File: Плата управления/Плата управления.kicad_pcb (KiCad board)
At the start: 2 copper layers, 66 x 58.4 mm, 65 parts, among them J1 Conn_01x10, J2 Conn_01x10, J3 Conn_01x02, J4 A, J5 B, J6 C, U1 LMV7239M5, U2 LMV324, U3 ISO1050DUB, U5 STM32F071V8Tx, U6 AS5047D, U7 AD8210

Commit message: Питание с (lib_symbols
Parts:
- added C21: 10u, Capacitor_SMD:C_1210_3225Metric_Pad1.33x2.70mm_HandSolder, F.Cu at (131.6, 93.0)
- added C22: 470n, Capacitor_SMD:C_0805_2012Metric_Pad1.18x1.45mm_HandSolder, F.Cu at (134.6, 92.5)
- added C23: 100n, Capacitor_SMD:C_0603_1608Metric_Pad1.08x0.95mm_HandSolder, F.Cu at (135.9, 88.4)
- added C24: 100n, Capacitor_SMD:C_0603_1608Metric_Pad1.08x0.95mm_HandSolder, F.Cu at (145.8, 88.2)
- added C25: 4.7u, Capacitor_SMD:C_0805_2012Metric_Pad1.18x1.45mm_HandSolder, F.Cu at (145.8, 96.3)
- added C26: 100n, Capacitor_SMD:C_0603_1608Metric_Pad1.08x0.95mm_HandSolder, F.Cu at (149.1, 91.9)
- added C27: 22u, Capacitor_SMD:C_1210_3225Metric_Pad1.33x2.70mm_HandSolder, F.Cu at (151.6, 92.7)
- added D7: TPS55165QPWPRQ1, Package_SO:HTSSOP-20-1EP_4.4x6.5mm_P0.65mm_EP3.4x6.5mm, F.Cu at (140.8, 91.7)
- added L1: 4.7u, Inductor_SMD:L_Murata_LQH55DN_5.7x5.0mm, F.Cu at (140.7, 83.6)
- added R28: 100k, Resistor_SMD:R_0603_1608Metric_Pad0.98x0.95mm_HandSolder, F.Cu at (147.3, 91.9)
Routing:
- net Net-(D7-L1): track 0.00 -> 9.26 mm
- net Net-(D7-L2): track 0.00 -> 8.99 mm
- net Net-(D7-VOS_FB): track 0.00 -> 7.43 mm
- net Net-(D7-PG): track 0.00 -> 3.90 mm
- net Net-(D7-BST1): track 0.00 -> 2.31 mm
- net Net-(D7-BST2): track 0.00 -> 2.16 mm
- net GND: track 0.00 -> 1.70 mm, vias 0 -> 1
- added copper zone on F.Cu, net GND
- added copper zone on F.Cu, net Net-(D7-IGN)
- added copper zone on F.Cu, net Net-(D7-VOUT)
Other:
- board size 66 x 58.4 mm -> 112.1 x 58.4 mm

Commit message: Питанипе с TPS55165QPWPRQ1
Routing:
- net Net-(D7-IGN): track 0.00 -> 4.06 mm
- net GND: track 1.70 -> 5.58 mm
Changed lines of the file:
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@@
   (gr_arc (start 116.205 94.615) (mid 113.015789 108.665562) (end 104.14 120.015)
     (stroke (width 0.1) (type default)) (layer "Edge.Cuts"))
+  (segment (start 131.572 94.565) (end 127.939 94.565) (width 0.5) (layer "F.Cu") (net 1))
   (segment (start 143.7675 93.3) (end 144.862 93.3) (width 0.25) (layer "F.Cu") (net 1))
   (segment (start 144.862 93.3) (end 145.288 93.726) (width 0.25) (layer "F.Cu") (net 1))
+  (segment (start 127.939 94.565) (end 127.762 94.742) (width 0.5) (layer "F.Cu") (net 1))
   (via (at 145.288 93.726) (size 0.8) (drill 0.4) (layers "F.Cu" "B.Cu") (net 1))
+  (segment (start 131.572 91.44) (end 127.508 91.44) (width 0.5) (layer "F.Cu") (net 168))
   (segment (start 136.398 83.566) (end 135.89 84.074) (width 0.5) (layer "F.Cu") (net 169))
   (segment (start 137.8675 89.41) (end 136.8925 89.41) (width 0.25) (layer "F.Cu") (net 169))

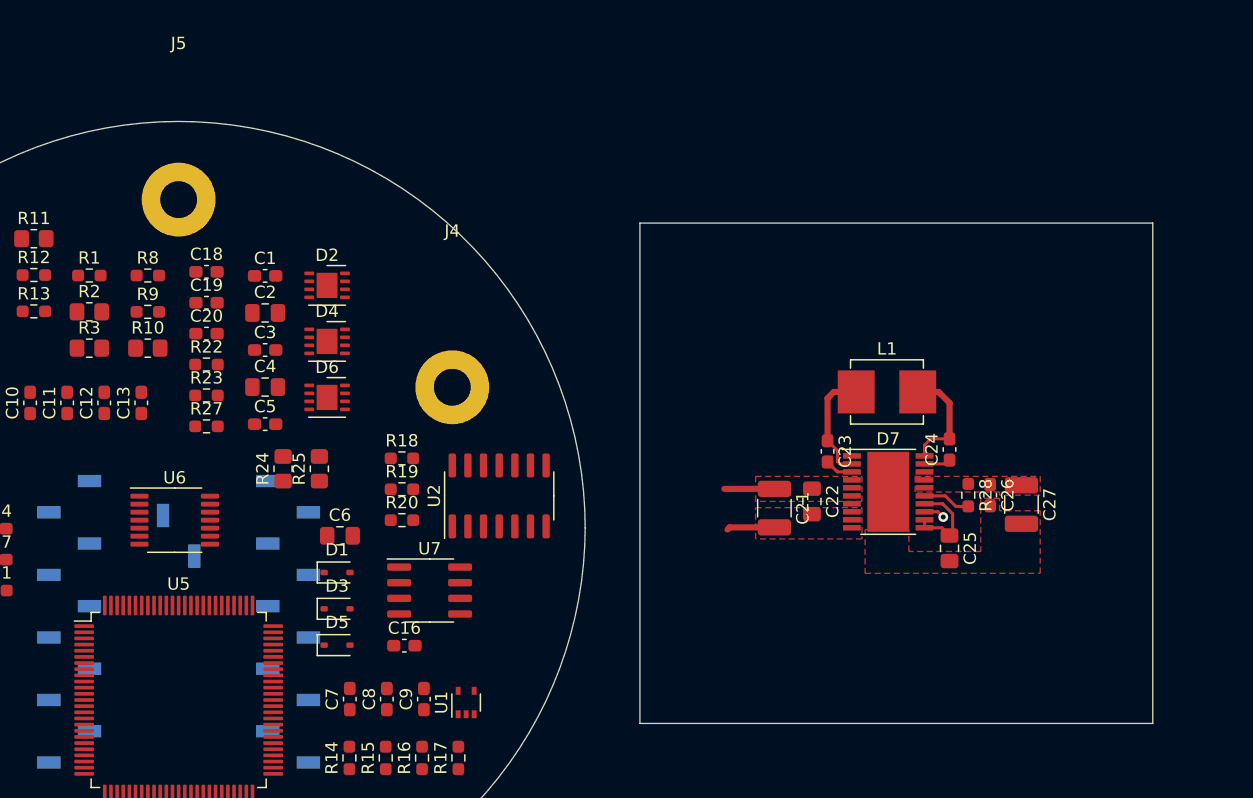
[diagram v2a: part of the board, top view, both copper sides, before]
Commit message: Поенял усилитель измерительный AD8210 на automotive исполнение INA283AID
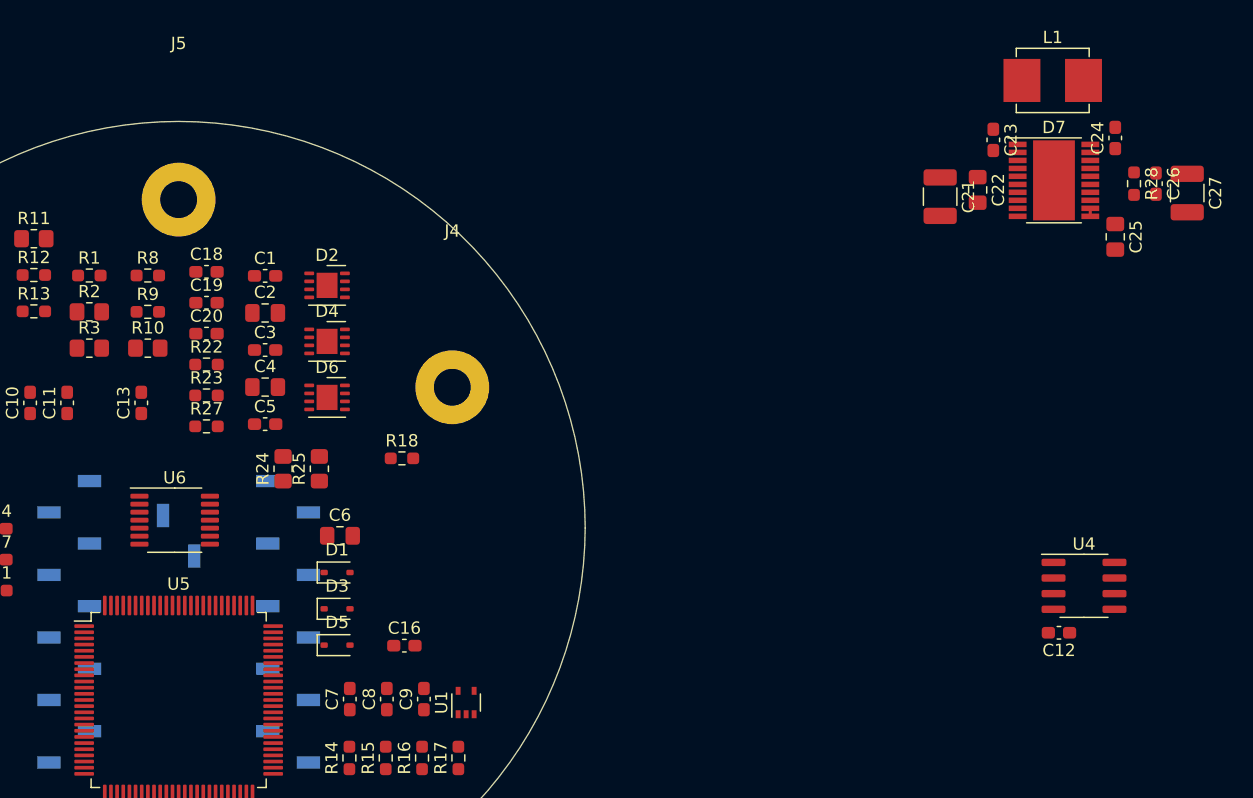
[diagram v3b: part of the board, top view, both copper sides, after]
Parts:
- removed R19: 1.6k, Resistor_SMD:R_0603_1608Metric_Pad0.98x0.95mm_HandSolder
- removed R20: 120, Resistor_SMD:R_0603_1608Metric_Pad0.98x0.95mm_HandSolder
- removed U2: LMV324, Package_SO:SOIC-14_3.9x8.7mm_P1.27mm
- removed U7: AD8210, Package_SO:SOIC-8_3.9x4.9mm_P1.27mm
- added U4: INA283, Package_SO:SOIC-8_3.9x4.9mm_P1.27mm, F.Cu at (156.7, 99.3)
- C12: value 56p -> 0.1u
- C16: value 0.1u -> 56p
- R18: value 1k -> 120
- moved C12 79.8 mm to (154.7, 103.1), turned to 180 degrees
- moved C25 28.7 mm to (159.3, 71.0)
- moved D7 28.7 mm to (154.3, 66.4)
- moved C24 28.7 mm to (159.3, 62.9)
- moved C23 28.7 mm to (149.4, 63.1)
- moved R28 28.7 mm to (160.8, 66.6)
- moved C22 28.7 mm to (148.1, 67.2)
- moved L1 28.7 mm to (154.2, 58.3)
- moved C21 28.7 mm to (145.0, 67.7)
- moved C26 28.7 mm to (162.6, 66.6)
- moved C27 28.7 mm to (165.1, 67.4)
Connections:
- C12 pad 1: DC_Current_MCU -> +3.3V
- C16 pad 1: GND -> DC_Current_MCU
- C16 pad 2: +5V -> GND
- D7 pad 21: GND -> (no net)
- R15 pad 1: +5V -> +3.3V
- R16 pad 2: Net-(R16-Pad2) -> DC_Current_MCU
- R18 pad 2: Net-(R16-Pad2) -> DC_Current_MCU
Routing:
- net Net-(D7-L1): track 9.26 -> 0.00 mm
- net Net-(D7-L2): track 8.99 -> 0.00 mm
- net Net-(D7-VOS_FB): track 7.43 -> 1.01 mm
- net GND: track 5.58 -> 0.00 mm, vias 1 -> 0
- net Net-(D7-IGN): track 4.06 -> 0.00 mm
- net Net-(D7-PG): track 3.90 -> 0.00 mm
- net Net-(D7-BST1): track 2.31 -> 0.00 mm
- net Net-(D7-BST2): track 2.16 -> 0.44 mm
- removed copper zone on F.Cu, net GND
- removed copper zone on F.Cu, net Net-(D7-IGN)
- removed copper zone on F.Cu, net Net-(D7-VOUT)
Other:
- board size 112.1 x 58.4 mm -> 66 x 58.4 mm

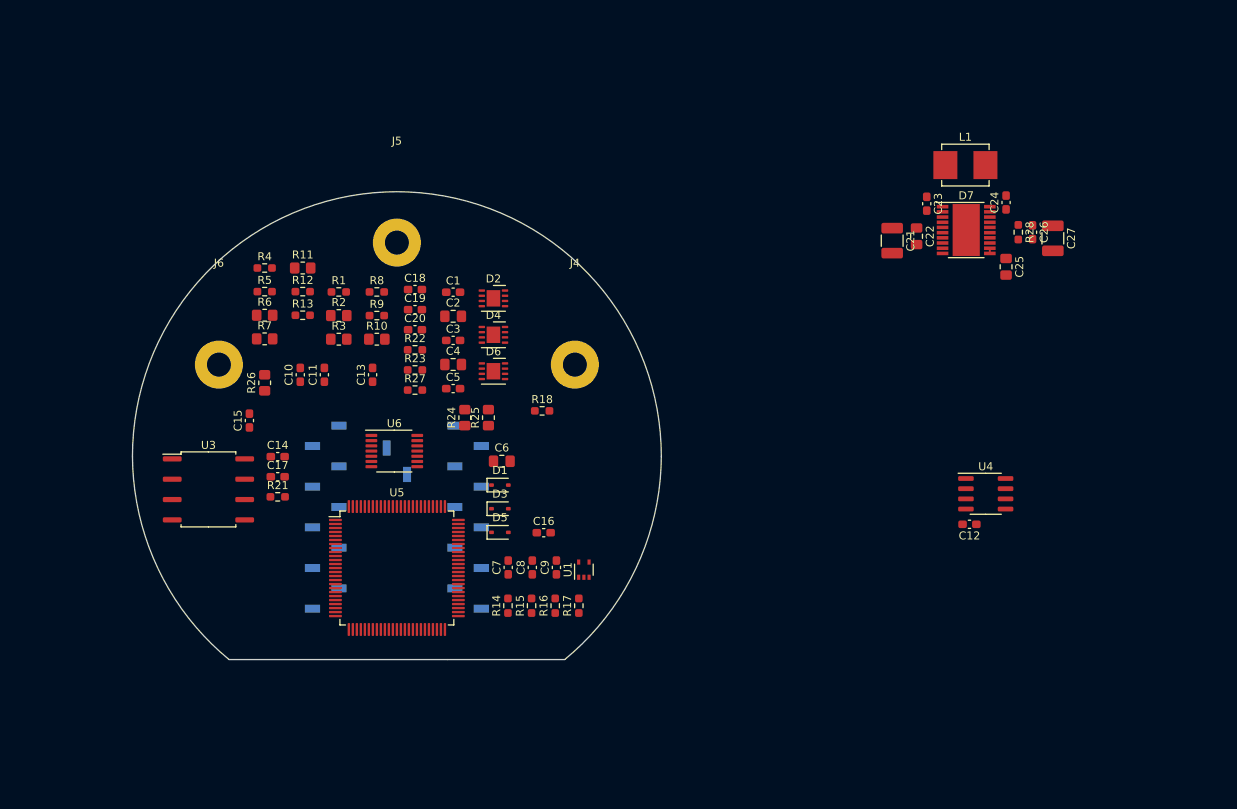
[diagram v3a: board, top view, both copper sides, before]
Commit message: Добавил питание 12В в automotive испорлнении и 3.3В
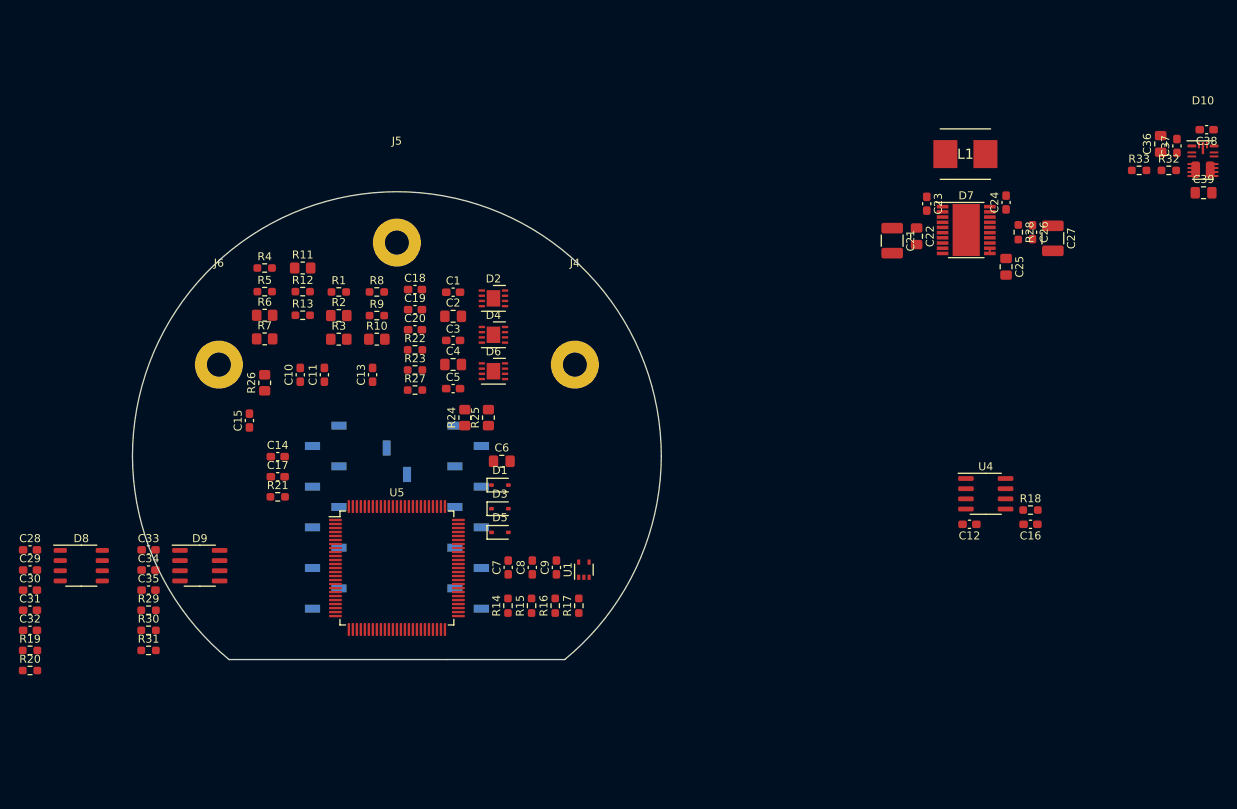
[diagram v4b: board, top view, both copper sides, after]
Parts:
- removed U3: ISO1050DUB, Package_SO:SOP-8_6.62x9.15mm_P2.54mm
- removed U6: AS5047D, Package_SO:TSSOP-14_4.4x5mm_P0.65mm
- added C28: 100n, Capacitor_SMD:C_0603_1608Metric_Pad1.08x0.95mm_HandSolder, F.Cu at (37.4, 106.3)
- added C29: 1n, Capacitor_SMD:C_0603_1608Metric_Pad1.08x0.95mm_HandSolder, F.Cu at (37.4, 108.8)
- added C30: 1n, Capacitor_SMD:C_0603_1608Metric_Pad1.08x0.95mm_HandSolder, F.Cu at (37.4, 111.3)
- added C31: 100n, Capacitor_SMD:C_0603_1608Metric_Pad1.08x0.95mm_HandSolder, F.Cu at (37.4, 113.9)
- added C32: 100n, Capacitor_SMD:C_0603_1608Metric_Pad1.08x0.95mm_HandSolder, F.Cu at (37.4, 116.4)
- added C33: 56p, Capacitor_SMD:C_0603_1608Metric_Pad1.08x0.95mm_HandSolder, F.Cu at (52.2, 106.3)
- added C34: 56p, Capacitor_SMD:C_0603_1608Metric_Pad1.08x0.95mm_HandSolder, F.Cu at (52.2, 108.8)
- added C35: 56p, Capacitor_SMD:C_0603_1608Metric_Pad1.08x0.95mm_HandSolder, F.Cu at (52.2, 111.3)
- added C36: 4.7u, Capacitor_SMD:C_0805_2012Metric_Pad1.18x1.45mm_HandSolder, F.Cu at (178.6, 55.6)
- added C37: 100n, Capacitor_SMD:C_0603_1608Metric_Pad1.08x0.95mm_HandSolder, F.Cu at (180.6, 55.9)
- added C38: 1u, Capacitor_SMD:C_0603_1608Metric_Pad1.08x0.95mm_HandSolder, F.Cu at (184.3, 53.8)
- added C39: 22u, Capacitor_SMD:C_0805_2012Metric_Pad1.18x1.45mm_HandSolder, F.Cu at (183.9, 61.7)
- added D10: TPSM33625, Convertor_DCDC_My:QFN-FCMOD, F.Cu at (183.8, 57.8)
- added D8: NSM3012, Package_SO:SOP-8_3.9x4.9mm_P1.27mm, F.Cu at (43.8, 108.3)
- added D9: SIT65HVD232DR, Package_SO:SOIC-8_3.9x4.9mm_P1.27mm, F.Cu at (58.6, 108.3)
- added R19: 10, Resistor_SMD:R_0603_1608Metric_Pad0.98x0.95mm_HandSolder, F.Cu at (37.4, 118.9)
- added R20: 50, Resistor_SMD:R_0603_1608Metric_Pad0.98x0.95mm_HandSolder, F.Cu at (37.4, 121.4)
- added R29: 10k, Resistor_SMD:R_0603_1608Metric_Pad0.98x0.95mm_HandSolder, F.Cu at (52.2, 113.9)
- added R30: 10k, Resistor_SMD:R_0603_1608Metric_Pad0.98x0.95mm_HandSolder, F.Cu at (52.2, 116.4)
- added R31: 10k, Resistor_SMD:R_0603_1608Metric_Pad0.98x0.95mm_HandSolder, F.Cu at (52.2, 118.9)
- added R32: 100k, Resistor_SMD:R_0603_1608Metric_Pad0.98x0.95mm_HandSolder, F.Cu at (179.6, 58.9)
- added R33: 100k, Resistor_SMD:R_0603_1608Metric_Pad0.98x0.95mm_HandSolder, F.Cu at (175.9, 58.9)
- L1: footprint Inductor_SMD:L_Murata_LQH55DN_5.7x5.0mm -> Inductor_my:LQH66SN100M03L
- moved R18 62.2 mm to (162.3, 101.3)
- moved C16 60.8 mm to (162.3, 103.1), turned to 180 degrees
- moved L1 1.37 mm to (154.2, 56.9)
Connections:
- C14 pad 2: +5V -> Net-(D9-D)
- C17 pad 2: +3.3V -> CANH
- C21 pad 1: Net-(D7-IGN) -> +24V
- C22 pad 1: Net-(D7-IGN) -> +24V
- C26 pad 1: Net-(D7-VOUT) -> +12V
- C27 pad 1: Net-(D7-VOUT) -> +12V
- D7 pad 16: Net-(D7-VOUT) -> +12V
- D7 pad 17: Net-(D7-VOUT) -> +12V
- D7 pad 4: Net-(D7-IGN) -> +24V
- D7 pad 5: Net-(D7-IGN) -> +24V
- D7 pad 6: Net-(D7-IGN) -> +24V
- R28 pad 1: Net-(D7-VOUT) -> +12V
